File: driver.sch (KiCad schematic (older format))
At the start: 45 parts, among them J1 Screw_Terminal_01x02, J2 Conn_02x12_Odd_Even, Q10 Q_NMOS_GDSD, Q11 Q_NMOS_GDSD, Q12 Q_NMOS_GDSD, Q13 Q_NMOS_GDSD, Q14 Q_NMOS_GDSD, Q15 Q_NMOS_GDSD, Q16 Q_NMOS_GDSD, Q17 IRF9Z34 PMOS_DGS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

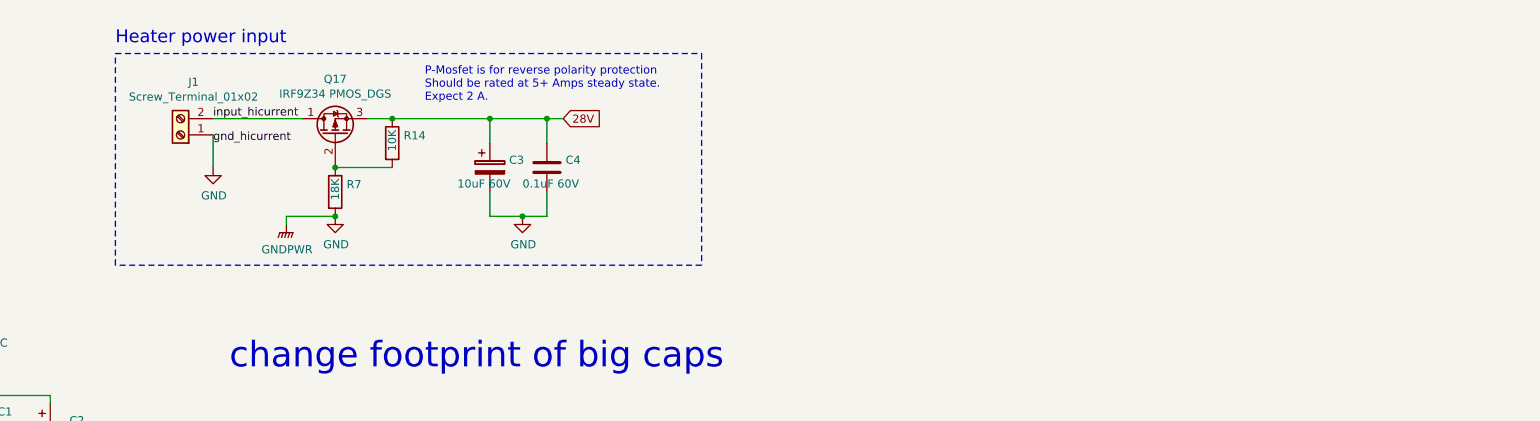
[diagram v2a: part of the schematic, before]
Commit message: Capacitor updates + voltage limit 50V + routing
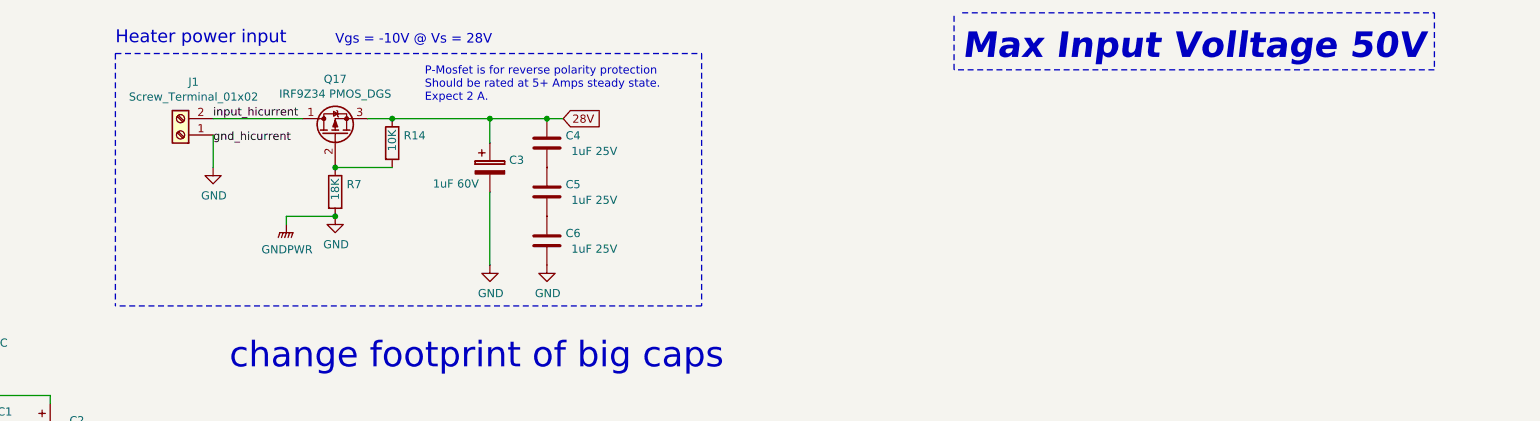
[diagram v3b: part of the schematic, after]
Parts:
- added C5, C6: 1uF 25V, Capacitor_SMD:C_1206_3216Metric_Pad1.42x1.75mm_HandSolder, symbol Device:C
- C2: footprint (none) -> Capacitor_THT:CP_Radial_D8.0mm_P3.80mm
- C3: value 10uF 60V -> 1uF 60V; footprint (none) -> Capacitor_THT:CP_Radial_D8.0mm_P3.80mm
- C4: value 0.1uF 60V -> 1uF 25V; footprint Capacitor_SMD:C_1210_3225Metric_Pad1.42x2.65mm_HandSolder -> Capacitor_SMD:C_1206_3216Metric_Pad1.42x1.75mm_HandSolder
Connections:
- net GND: now also C6.2; no longer C4.2
- new net: C4.2, C5.1
- new net: C5.2, C6.1
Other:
- note added: "Max Input Volltage 50V"
- note added: "Vgs = -10V @ Vs = 28V"
- moved on the sheet: C4
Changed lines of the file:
@@
 F 0 "C2" H 7268 3296 50  0000 L CNN
 F 1 "1uF" H 7268 3205 50  0000 L CNN
-F 2 "" H 7188 3100 50  0001 C CNN
+F 2 "Capacitor_THT:CP_Radial_D8.0mm_P3.80mm" H 7188 3100 50  0001 C CNN
 F 3 "~" H 7150 3250 50  0001 C CNN
 	1    7150 3250
@@
 L power:GND #PWR021
 U 1 1 5C43FABC
-P 10050 1950
-F 0 "#PWR021" H 10050 1700 50  0001 C CNN
-F 1 "GND" H 10055 1777 50  0000 C CNN
-F 2 "" H 10050 1950 50  0001 C CNN
-F 3 "" H 10050 1950 50  0001 C CNN
-	1    10050 1950
+P 9850 2250
+F 0 "#PWR021" H 9850 2000 50  0001 C CNN
+F 1 "GND" H 9855 2077 50  0000 C CNN
+F 2 "" H 9850 2250 50  0001 C CNN
+F 3 "" H 9850 2250 50  0001 C CNN
+	1    9850 2250
 	1    0    0    -1
 $EndComp
@@
 P 9850 1650
 F 0 "C3" H 9968 1696 50  0000 L CNN
-F 1 "10uF 60V" H 9650 1550 50  0000 L CNN
-F 2 "" H 9888 1500 50  0001 C CNN
+F 1 "1uF 60V" H 9500 1550 50  0000 L CNN
+F 2 "Capacitor_THT:CP_Radial_D8.0mm_P3.80mm" H 9888 1500 50  0001 C CNN
 F 3 "~" H 9850 1650 50  0001 C CNN
 	1    9850 1650
@@
 L Device:C C4
 U 1 1 5C4A5A2A
-P 10200 1650
-F 0 "C4" H 10315 1696 50  0000 L CNN
-F 1 "0.1uF 60V" H 10050 1550 50  0000 L CNN
-F 2 "Capacitor_SMD:C_1210_3225Metric_Pad1.42x2.65mm_HandSolder" H 10238 1500 50  0001 C CNN
-F 3 "~" H 10200 1650 50  0001 C CNN
-	1    10200 1650
-	1    0    0    -1
-$EndComp
-Wire Wire Line
-	10200 1500 10200 1350
-Connection ~ 10200 1350
-Wire Wire Line
-	10200 1350 10300 1350
+P 10200 1500
+F 0 "C4" H 10315 1546 50  0000 L CNN
+F 1 "1uF 25V" H 10350 1450 50  0000 L CNN
+F 2 "Capacitor_SMD:C_1206_3216Metric_Pad1.42x1.75mm_HandSolder" H 10238 1350 50  0001 C CNN
+F 3 "~" H 10200 1500 50  0001 C CNN
+	1    10200 1500
+	1    0    0    -1
+$EndComp
 Wire Wire Line
 	9850 1500 9850 1350
 Connection ~ 9850 1350
-Wire Wire Line
-	9850 1350 10200 1350
-Wire Wire Line
-	9850 1800 9850 1950
-Wire Wire Line
-	10050 1950 10200 1950
-Wire Wire Line
-	10200 1950 10200 1800
 $Comp
 L Device:R R3
@@
 	7550 950  11150 950
 Wire Notes Line
-	11150 950  11150 2250
-Wire Notes Line
-	11150 2250 7550 2250
-Wire Notes Line
-	7550 2250 7550 950
-Wire Notes Line
 	10000 5250 10000 6950
 Wire Notes Line
@@
 Wire Notes Line
 	11500 5250 10000 5250
-Wire Wire Line
-	6500 1850 6500 2350
 Wire Wire Line
 	9100 1350 9250 1350
@@
 Wire Wire Line
 	8650 7750 8650 7800
-Connection ~ 10050 1950
-Wire Wire Line
-	9850 1950 10050 1950
+Text Notes 8900 900  0    59   ~ 0
+Vgs = -10V @ Vs = 28V
+Wire Wire Line
+	6500 1850 6500 2350
+Wire Wire Line
+	9850 1800 9850 2250
+Text Notes 12750 1000 0    157  Italic 31
+Max Input Volltage 50V
+Wire Notes Line
+	12750 700  15650 700
+Wire Notes Line
+	15650 700  15650 1050
+Wire Notes Line
+	15650 1050 12700 1050
+Wire Notes Line
+	12700 1050 12700 700
+Wire Wire Line
+	9850 1350 10200 1350
+Connection ~ 10200 1350
+Wire Wire Line
+	10200 1350 10300 1350
+$Comp
+L power:GND #PWR01
+U 1 1 5C5219C2
+P 10200 2250
+F 0 "#PWR01" H 10200 2000 50  0001 C CNN
+F 1 "GND" H 10205 2077 50  0000 C CNN
+F 2 "" H 10200 2250 50  0001 C CNN
+F 3 "" H 10200 2250 50  0001 C CNN
+	1    10200 2250
+	1    0    0    -1
+$EndComp
+$Comp
+L Device:C C5
+U 1 1 5C521F30
+P 10200 1800
+F 0 "C5" H 10315 1846 50  0000 L CNN
+F 1 "1uF 25V" H 10350 1750 50  0000 L CNN
+F 2 "Capacitor_SMD:C_1206_3216Metric_Pad1.42x1.75mm_HandSolder" H 10238 1650 50  0001 C CNN
+F 3 "~" H 10200 1800 50  0001 C CNN
+	1    10200 1800
+	1    0    0    -1
+$EndComp
+$Comp
+L Device:C C6
+U 1 1 5C521FA8
+P 10200 2100
+F 0 "C6" H 10315 2146 50  0000 L CNN
+F 1 "1uF 25V" H 10350 2050 50  0000 L CNN
+F 2 "Capacitor_SMD:C_1206_3216Metric_Pad1.42x1.75mm_HandSolder" H 10238 1950 50  0001 C CNN
+F 3 "~" H 10200 2100 50  0001 C CNN
+	1    10200 2100
+	1    0    0    -1
+$EndComp
+Wire Notes Line
+	11150 2500 7550 2500
+Wire Notes Line
+	11150 950  11150 2500
+Wire Notes Line
+	7550 950  7550 2500
 Wire Wire Line
 	6400 1850 6400 2350

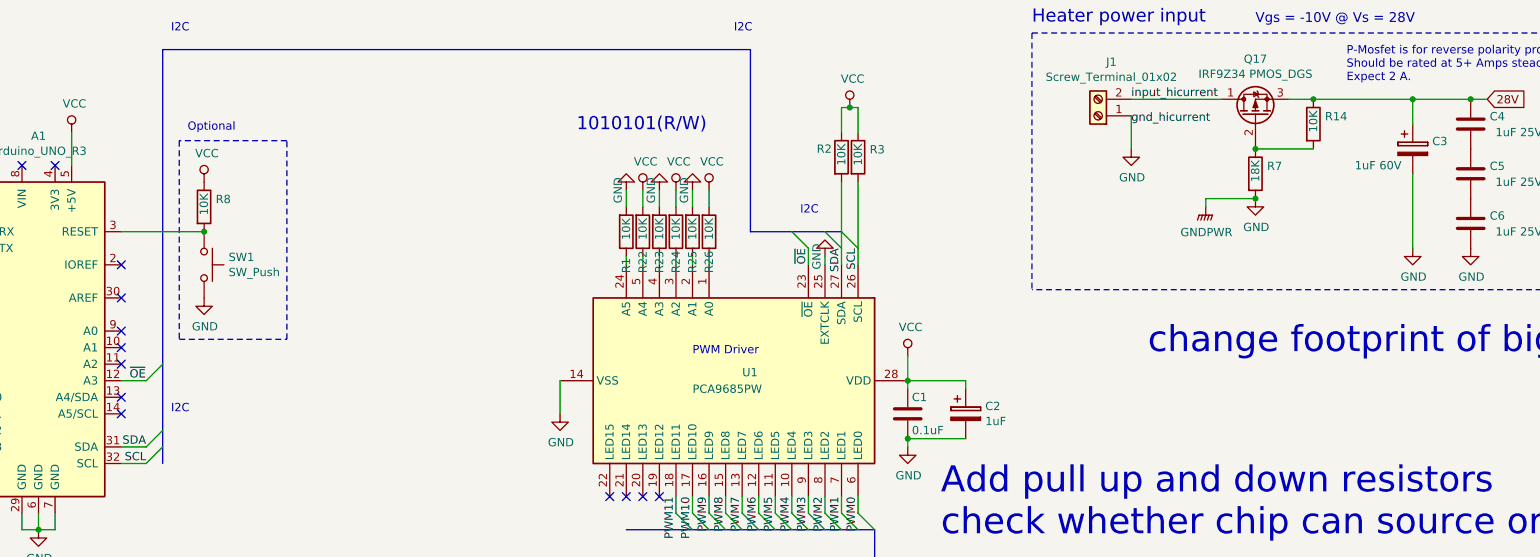
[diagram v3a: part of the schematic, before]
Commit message: Remove reset button, finalize capacitor sizes
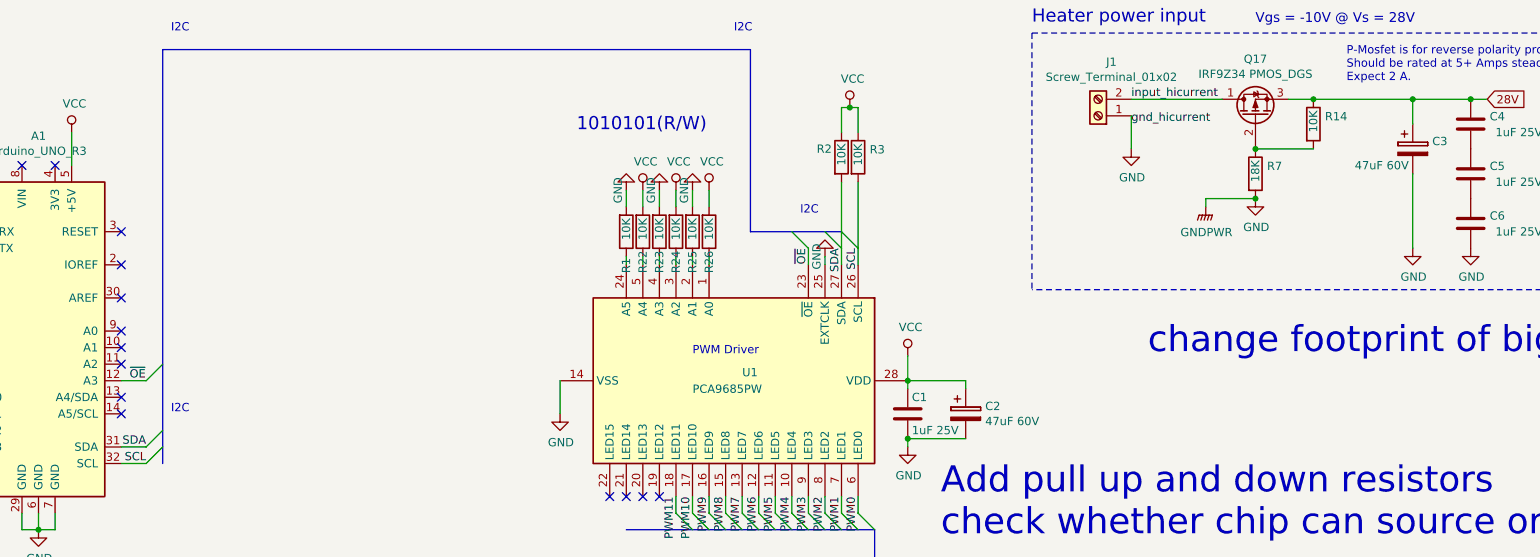
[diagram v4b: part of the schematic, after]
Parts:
- removed R8: 10K, Resistor_SMD:R_0805_2012Metric_Pad1.15x1.40mm_HandSolder, symbol Device:R
- removed SW1: SW_Push, Button_Switch_SMD:SW_SPST_B3S-1000, symbol Switch:SW_Push
- C1: value 0.1uF -> 1uF 25V; footprint Capacitor_SMD:C_1210_3225Metric_Pad1.42x2.65mm_HandSolder -> Capacitor_SMD:C_1206_3216Metric_Pad1.42x1.75mm_HandSolder
- C2: value 1uF -> 47uF 60V; footprint Capacitor_THT:CP_Radial_D8.0mm_P3.80mm -> Capacitor_THT:CP_Radial_D6.3mm_P2.50mm
- C3: value 1uF 60V -> 47uF 60V; footprint Capacitor_THT:CP_Radial_D8.0mm_P3.80mm -> Capacitor_THT:CP_Radial_D6.3mm_P2.50mm
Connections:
- no-connect marks 27 -> 28
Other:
- note removed: "Optional"
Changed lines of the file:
@@
 P 6800 3250
 F 0 "C1" H 6825 3350 50  0000 L CNN
-F 1 "0.1uF" H 6825 3150 50  0000 L CNN
-F 2 "Capacitor_SMD:C_1210_3225Metric_Pad1.42x2.65mm_HandSolder" H 6838 3100 50  0001 C CNN
+F 1 "1uF 25V" H 6825 3150 50  0000 L CNN
+F 2 "Capacitor_SMD:C_1206_3216Metric_Pad1.42x1.75mm_HandSolder" H 6838 3100 50  0001 C CNN
 F 3 "~" H 6800 3250 50  0001 C CNN
 	1    6800 3250
@@
 P 7150 3250
 F 0 "C2" H 7268 3296 50  0000 L CNN
-F 1 "1uF" H 7268 3205 50  0000 L CNN
-F 2 "Capacitor_THT:CP_Radial_D8.0mm_P3.80mm" H 7188 3100 50  0001 C CNN
+F 1 "47uF 60V" H 7268 3205 50  0000 L CNN
+F 2 "Capacitor_THT:CP_Radial_D6.3mm_P2.50mm" H 7188 3100 50  0001 C CNN
 F 3 "~" H 7150 3250 50  0001 C CNN
 	1    7150 3250
@@
 Wire Wire Line
 	7250 6150 7350 6150
-$Comp
-L Switch:SW_Push SW1
-U 1 1 5C4BAB0E
-P 2550 2350
-F 0 "SW1" V 2504 2498 50  0000 L CNN
-F 1 "SW_Push" V 2595 2498 50  0000 L CNN
-F 2 "Button_Switch_SMD:SW_SPST_B3S-1000" H 2550 2550 50  0001 C CNN
-F 3 "" H 2550 2550 50  0001 C CNN
-	1    2550 2350
-	0    1    1    0
-$EndComp
-Wire Wire Line
-	2050 2150 2550 2150
-$Comp
-L power:VCC #PWR0102
-U 1 1 5C4BD6AC
-P 2550 1850
-F 0 "#PWR0102" H 2550 1700 50  0001 C CNN
-F 1 "VCC" H 2567 2023 50  0000 C CNN
-F 2 "" H 2550 1850 50  0001 C CNN
-F 3 "" H 2550 1850 50  0001 C CNN
-	1    2550 1850
-	1    0    0    -1
-$EndComp
-$Comp
-L Device:R R8
-U 1 1 5C4BD73F
-P 2550 2000
-F 0 "R8" H 2620 2046 50  0000 L CNN
-F 1 "10K" V 2550 1950 50  0000 L CNN
-F 2 "Resistor_SMD:R_0805_2012Metric_Pad1.15x1.40mm_HandSolder" V 2480 2000 50  0001 C CNN
-F 3 "~" H 2550 2000 50  0001 C CNN
-	1    2550 2000
-	1    0    0    -1
-$EndComp
-Connection ~ 2550 2150
-$Comp
-L power:GND #PWR0103
-U 1 1 5C4BDB37
-P 2550 2550
-F 0 "#PWR0103" H 2550 2300 50  0001 C CNN
-F 1 "GND" H 2555 2377 50  0000 C CNN
-F 2 "" H 2550 2550 50  0001 C CNN
-F 3 "" H 2550 2550 50  0001 C CNN
-	1    2550 2550
-	1    0    0    -1
-$EndComp
 Text Notes 9450 1250 0    50   ~ 0
 P-Mosfet is for reverse polarity protection\nShould be rated at 5+ Amps steady state.\nExpect 2 A.
@@
 Text Notes 2350 3250 0    50   ~ 0
 I2C
-Text Notes 2450 1550 0    50   ~ 0
-Optional
 Text Notes 5650 4200 0    50   ~ 0
 PWM channels
@@
 P 9850 1650
 F 0 "C3" H 9968 1696 50  0000 L CNN
-F 1 "1uF 60V" H 9500 1550 50  0000 L CNN
-F 2 "Capacitor_THT:CP_Radial_D8.0mm_P3.80mm" H 9888 1500 50  0001 C CNN
+F 1 "47uF 60V" H 9500 1550 50  0000 L CNN
+F 2 "Capacitor_THT:CP_Radial_D6.3mm_P2.50mm" H 9888 1500 50  0001 C CNN
 F 3 "~" H 9850 1650 50  0001 C CNN
 	1    9850 1650
@@
 NoConn ~ 5000 3750
 NoConn ~ 5300 3750
-Wire Notes Line
-	2400 1600 2400 2800
-Wire Notes Line
-	2400 2800 3050 2800
-Wire Notes Line
-	3050 2800 3050 1600
-Wire Notes Line
-	3050 1600 2400 1600
 Wire Notes Line
 	7550 950  11150 950
@@
 Wire Notes Line
 	7550 950  7550 2500
+NoConn ~ 2050 2150
 Wire Wire Line
 	6400 1850 6400 2350
